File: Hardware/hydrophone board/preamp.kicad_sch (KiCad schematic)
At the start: 10 parts, among them U302 AD8541ARTZ

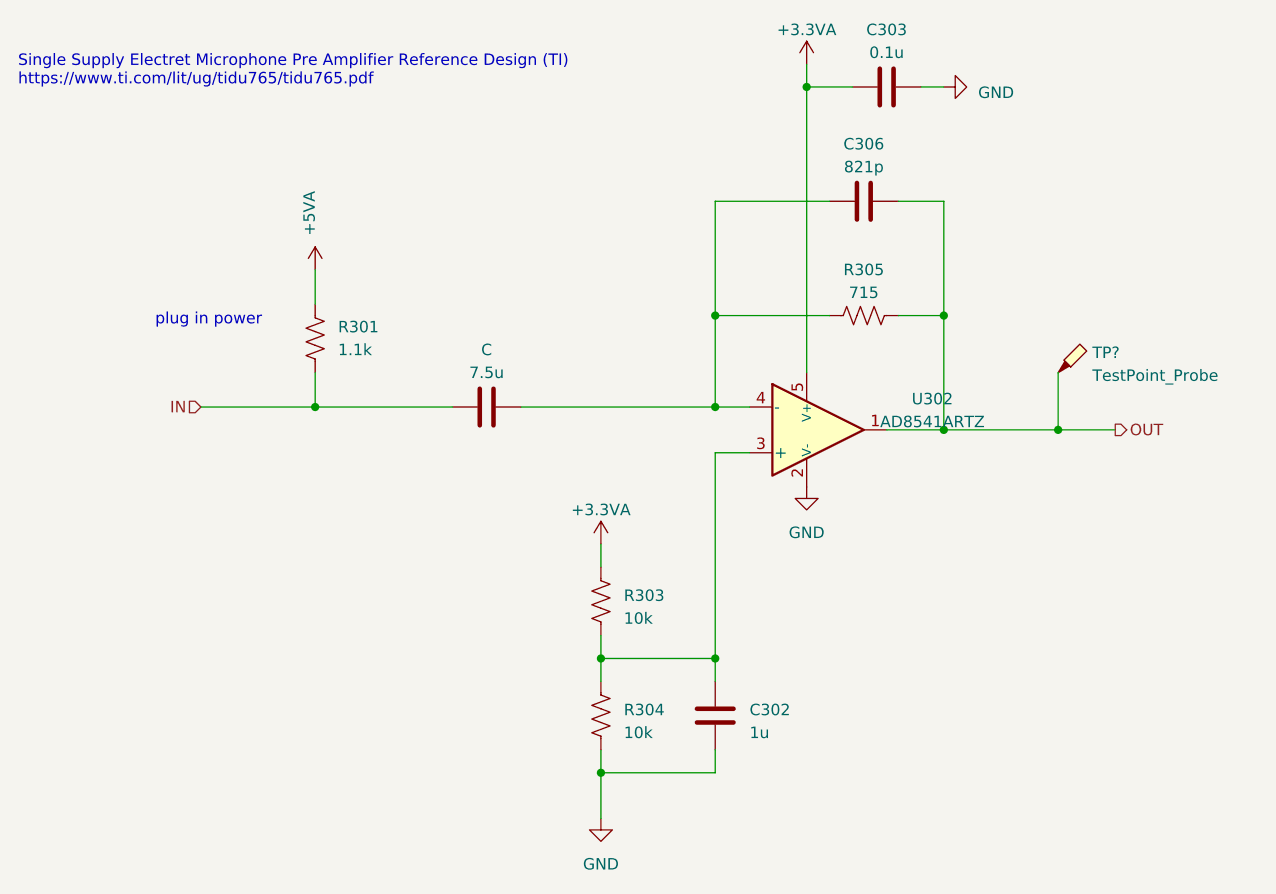
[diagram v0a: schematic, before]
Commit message: added teensy footprint
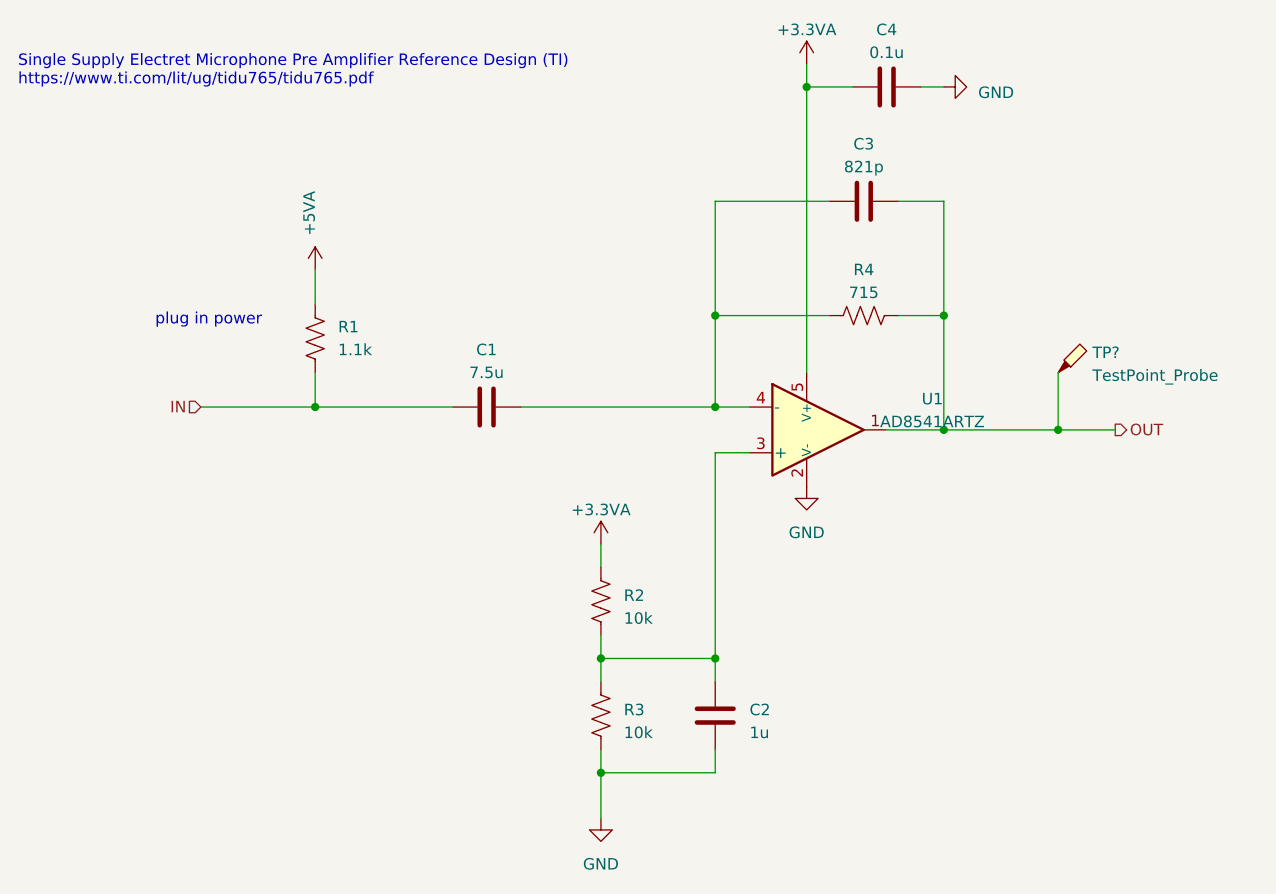
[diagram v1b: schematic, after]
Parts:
- renumbered C to C1, C302 to C2, C306 to C3, C303 to C4, R301 to R1, R303 to R2, R304 to R3, R305 to R4, U302 to U1
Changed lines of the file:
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@@
   (symbol (lib_id "power:+5VA") (at 63.5 71.12 0) (unit 1)
     (in_bom yes) (on_board yes) (dnp no) (fields_autoplaced)
-    (property "Reference" "#PWR0301" (at 63.5 74.93 0)
+    (property "Reference" "#PWR03" (at 63.5 74.93 0)
       (effects (font (size 1.27 1.27)) hide)
     )
@@
       (project "hydrophone board"
         (path "/4356d3a6-6a00-447d-897e-473f60221539/f560d530-135c-40dc-9144-4f9599a30f13"
-          (reference "#PWR0301") (unit 1)
+          (reference "#PWR03") (unit 1)
         )
       )
@@
   (symbol (lib_id "Device:C") (at 124.46 63.5 270) (unit 1)
     (in_bom yes) (on_board yes) (dnp no) (fields_autoplaced)
-    (property "Reference" "C306" (at 124.46 57.15 90)
+    (property "Reference" "C3" (at 124.46 57.15 90)
       (effects (font (size 1.27 1.27)))
     )
@@
       (project "hydrophone board"
         (path "/4356d3a6-6a00-447d-897e-473f60221539/f560d530-135c-40dc-9144-4f9599a30f13"
-          (reference "C306") (unit 1)
+          (reference "C3") (unit 1)
         )
       )
@@
         )
         (path "/4356d3a6-6a00-447d-897e-473f60221539/f560d530-135c-40dc-9144-4f9599a30f13"
-          (reference "#PWR0302") (unit 1)
+          (reference "#PWR04") (unit 1)
         )
       )
@@
         )
         (path "/4356d3a6-6a00-447d-897e-473f60221539/f560d530-135c-40dc-9144-4f9599a30f13"
-          (reference "#PWR0304") (unit 1)
+          (reference "#PWR06") (unit 1)
         )
       )
@@
   (symbol (lib_id "Device:R_US") (at 95.25 107.95 0) (unit 1)
     (in_bom yes) (on_board yes) (dnp no) (fields_autoplaced)
-    (property "Reference" "R303" (at 97.79 107.315 0)
+    (property "Reference" "R2" (at 97.79 107.315 0)
       (effects (font (size 1.27 1.27)) (justify left))
     )
@@
       (project "hydrophone board"
         (path "/4356d3a6-6a00-447d-897e-473f60221539/f560d530-135c-40dc-9144-4f9599a30f13"
-          (reference "R303") (unit 1)
+          (reference "R2") (unit 1)
         )
       )
@@
         )
         (path "/4356d3a6-6a00-447d-897e-473f60221539/f560d530-135c-40dc-9144-4f9599a30f13"
-          (reference "#PWR0305") (unit 1)
+          (reference "#PWR05") (unit 1)
         )
       )
@@
   (symbol (lib_id "Device:R_US") (at 124.46 76.2 90) (unit 1)
     (in_bom yes) (on_board yes) (dnp no) (fields_autoplaced)
-    (property "Reference" "R305" (at 124.46 71.12 90)
+    (property "Reference" "R4" (at 124.46 71.12 90)
       (effects (font (size 1.27 1.27)))
     )
@@
       (project "hydrophone board"
         (path "/4356d3a6-6a00-447d-897e-473f60221539/f560d530-135c-40dc-9144-4f9599a30f13"
-          (reference "R305") (unit 1)
+          (reference "R4") (unit 1)
         )
       )
@@
   (symbol (lib_id "Device:C") (at 82.55 86.36 90) (unit 1)
     (in_bom yes) (on_board yes) (dnp no) (fields_autoplaced)
-    (property "Reference" "C" (at 82.55 80.01 90)
+    (property "Reference" "C1" (at 82.55 80.01 90)
       (effects (font (size 1.27 1.27)))
     )
@@
       (project "hydrophone board"
         (path "/4356d3a6-6a00-447d-897e-473f60221539/f560d530-135c-40dc-9144-4f9599a30f13"
-          (reference "C") (unit 1)
+          (reference "C1") (unit 1)
         )
       )
@@
         )
         (path "/4356d3a6-6a00-447d-897e-473f60221539/f560d530-135c-40dc-9144-4f9599a30f13"
-          (reference "#PWR0303") (unit 1)
+          (reference "#PWR07") (unit 1)
         )
       )
@@
   (symbol (lib_id "Device:C") (at 107.95 120.65 180) (unit 1)
     (in_bom yes) (on_board yes) (dnp no) (fields_autoplaced)
-    (property "Reference" "C302" (at 111.76 120.015 0)
+    (property "Reference" "C2" (at 111.76 120.015 0)
       (effects (font (size 1.27 1.27)) (justify right))
     )
@@
       (project "hydrophone board"
         (path "/4356d3a6-6a00-447d-897e-473f60221539/f560d530-135c-40dc-9144-4f9599a30f13"
-          (reference "C302") (unit 1)
+          (reference "C2") (unit 1)
         )
       )
@@
   (symbol (lib_id "PCM_Amplifier_Operational_AKL:AD8541ARTZ") (at 119.38 88.9 0) (unit 1)
     (in_bom yes) (on_board yes) (dnp no) (fields_autoplaced)
-    (property "Reference" "U302" (at 132.08 85.4711 0)
+    (property "Reference" "U1" (at 132.08 85.4711 0)
       (effects (font (size 1.27 1.27)))
     )
@@
       (project "hydrophone board"
         (path "/4356d3a6-6a00-447d-897e-473f60221539/f560d530-135c-40dc-9144-4f9599a30f13"
-          (reference "U302") (unit 1)
+          (reference "U1") (unit 1)
         )
       )
@@
         )
         (path "/4356d3a6-6a00-447d-897e-473f60221539/f560d530-135c-40dc-9144-4f9599a30f13"
-          (reference "#PWR0307") (unit 1)
+          (reference "#PWR08") (unit 1)
         )
       )
@@
   (symbol (lib_id "Device:C") (at 127 50.8 90) (unit 1)
     (in_bom yes) (on_board yes) (dnp no) (fields_autoplaced)
-    (property "Reference" "C303" (at 127 44.45 90)
+    (property "Reference" "C4" (at 127 44.45 90)
       (effects (font (size 1.27 1.27)))
     )
@@
       (project "hydrophone board"
         (path "/4356d3a6-6a00-447d-897e-473f60221539/f560d530-135c-40dc-9144-4f9599a30f13"
-          (reference "C303") (unit 1)
+          (reference "C4") (unit 1)
         )
       )
@@
         )
         (path "/4356d3a6-6a00-447d-897e-473f60221539/f560d530-135c-40dc-9144-4f9599a30f13"
-          (reference "TP301") (unit 1)
+          (reference "TP1") (unit 1)
         )
       )
@@
   (symbol (lib_id "Device:R_US") (at 63.5 78.74 180) (unit 1)
     (in_bom yes) (on_board yes) (dnp no)
-    (property "Reference" "R301" (at 66.04 77.47 0)
+    (property "Reference" "R1" (at 66.04 77.47 0)
       (effects (font (size 1.27 1.27)) (justify right))
     )
@@
       (project "hydrophone board"
         (path "/4356d3a6-6a00-447d-897e-473f60221539/f560d530-135c-40dc-9144-4f9599a30f13"
-          (reference "R301") (unit 1)
+          (reference "R1") (unit 1)
         )
       )
@@
   (symbol (lib_id "Device:R_US") (at 95.25 120.65 0) (unit 1)
     (in_bom yes) (on_board yes) (dnp no) (fields_autoplaced)
-    (property "Reference" "R304" (at 97.79 120.015 0)
+    (property "Reference" "R3" (at 97.79 120.015 0)
       (effects (font (size 1.27 1.27)) (justify left))
     )
@@
       (project "hydrophone board"
         (path "/4356d3a6-6a00-447d-897e-473f60221539/f560d530-135c-40dc-9144-4f9599a30f13"
-          (reference "R304") (unit 1)
-        )
-      )
+          (reference "R3") (unit 1)
+        )
+      )

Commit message: annotate all component
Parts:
- renumbered C4 to C111, C3 to C112, C1 to C113, C2 to C114, R4 to R111, R1 to R112, R2 to R113, R3 to R114, U1 to U111

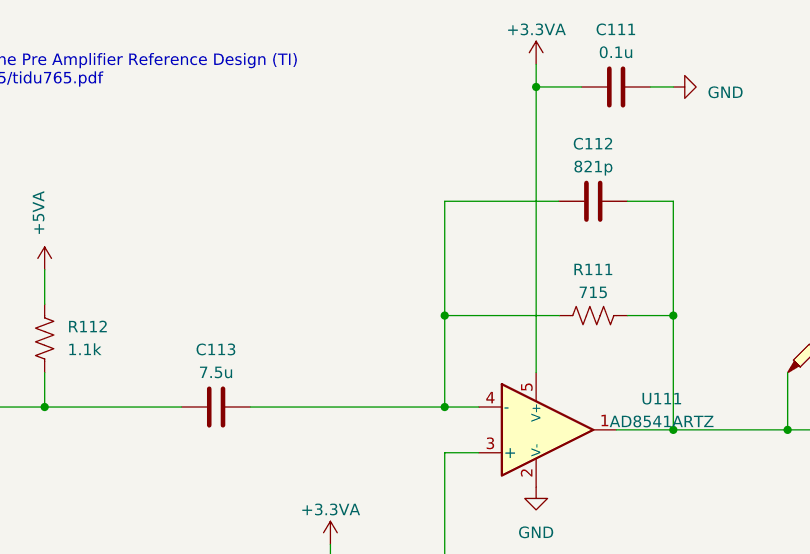
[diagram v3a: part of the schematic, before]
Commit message: assigned footprints
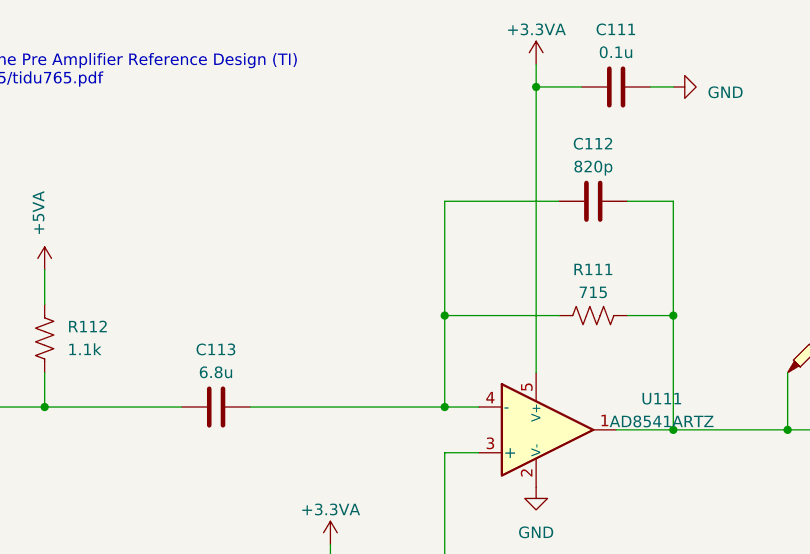
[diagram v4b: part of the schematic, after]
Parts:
- C111, C114: footprint (none) -> Capacitor_SMD:C_0603_1608Metric
- C112: value 821p -> 820p; footprint (none) -> Capacitor_SMD:C_0603_1608Metric
- C113: value 7.5u -> 6.8u; footprint (none) -> Capacitor_SMD:C_0805_2012Metric
- R111, R112, R113, R114: footprint (none) -> Resistor_SMD:R_0603_1608Metric
- TP?: footprint (none) -> Connector_PinHeader_2.54mm:PinHeader_1x01_P2.54mm_Vertical
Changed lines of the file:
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@@
       (effects (font (size 1.27 1.27)))
     )
-    (property "Value" "821p" (at 124.46 59.69 90)
-      (effects (font (size 1.27 1.27)))
-    )
-    (property "Footprint" "" (at 120.65 64.4652 0)
+    (property "Value" "820p" (at 124.46 59.69 90)
+      (effects (font (size 1.27 1.27)))
+    )
+    (property "Footprint" "Capacitor_SMD:C_0603_1608Metric" (at 120.65 64.4652 0)
       (effects (font (size 1.27 1.27)) hide)
     )
@@
       (effects (font (size 1.27 1.27)) (justify left))
     )
-    (property "Footprint" "" (at 96.266 108.204 90)
+    (property "Footprint" "Resistor_SMD:R_0603_1608Metric" (at 96.266 108.204 90)
       (effects (font (size 1.27 1.27)) hide)
     )
@@
       (effects (font (size 1.27 1.27)))
     )
-    (property "Footprint" "" (at 124.714 75.184 90)
+    (property "Footprint" "Resistor_SMD:R_0603_1608Metric" (at 124.714 75.184 90)
       (effects (font (size 1.27 1.27)) hide)
     )
@@
       (effects (font (size 1.27 1.27)))
     )
-    (property "Value" "7.5u" (at 82.55 82.55 90)
-      (effects (font (size 1.27 1.27)))
-    )
-    (property "Footprint" "" (at 86.36 85.3948 0)
+    (property "Value" "6.8u" (at 82.55 82.55 90)
+      (effects (font (size 1.27 1.27)))
+    )
+    (property "Footprint" "Capacitor_SMD:C_0805_2012Metric" (at 86.36 85.3948 0)
       (effects (font (size 1.27 1.27)) hide)
     )
@@
       (effects (font (size 1.27 1.27)) (justify right))
     )
-    (property "Footprint" "" (at 106.9848 116.84 0)
+    (property "Footprint" "Capacitor_SMD:C_0603_1608Metric" (at 106.9848 116.84 0)
       (effects (font (size 1.27 1.27)) hide)
     )
@@
       (effects (font (size 1.27 1.27)))
     )
-    (property "Footprint" "" (at 130.81 49.8348 0)
+    (property "Footprint" "Capacitor_SMD:C_0603_1608Metric" (at 130.81 49.8348 0)
       (effects (font (size 1.27 1.27)) hide)
     )
@@
       (effects (font (size 1.27 1.27)) (justify left))
     )
-    (property "Footprint" "" (at 151.13 82.55 0)
+    (property "Footprint" "Connector_PinHeader_2.54mm:PinHeader_1x01_P2.54mm_Vertical" (at 151.13 82.55 0)
       (effects (font (size 1.27 1.27)) hide)
     )
@@
       (effects (font (size 1.27 1.27)) (justify right))
     )
-    (property "Footprint" "" (at 62.484 78.486 90)
+    (property "Footprint" "Resistor_SMD:R_0603_1608Metric" (at 62.484 78.486 90)
       (effects (font (size 1.27 1.27)) hide)
     )
@@
       (effects (font (size 1.27 1.27)) (justify left))
     )
-    (property "Footprint" "" (at 96.266 120.904 90)
-      (effects (font (size 1.27 1.27)) hide)
-    )
+    (property "Footprint" "Resistor_SMD:R_0603_1608Metric" (at 96.266 120.904 90)
+      (effects (font (size 1.27 1.27)) hide)
+    )

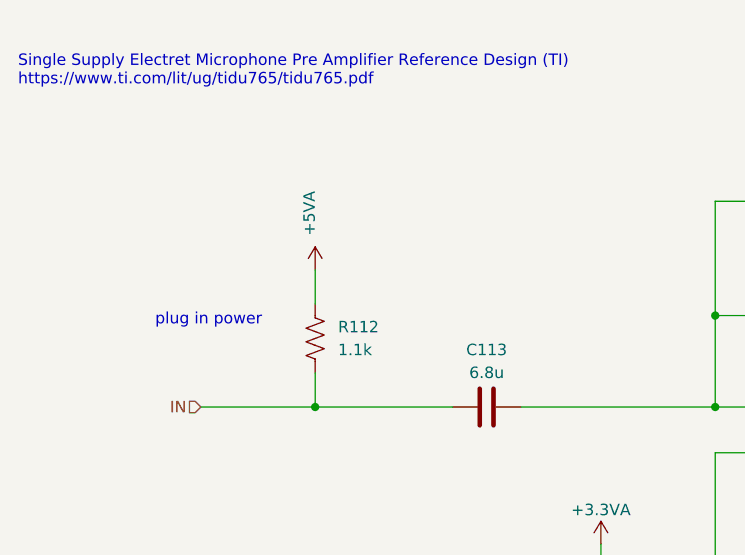
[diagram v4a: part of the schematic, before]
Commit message: resolved ERC errors and changed mic bias resistor for 3.3V
1.1k -> 360 ohm
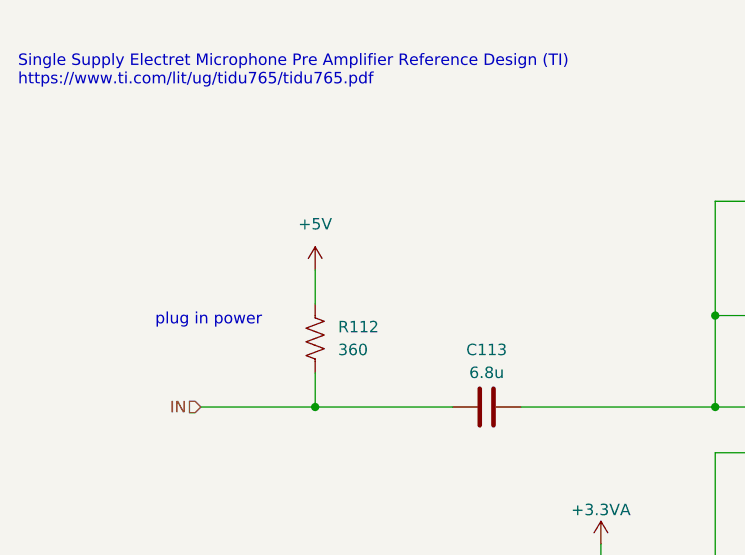
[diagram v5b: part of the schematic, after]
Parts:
- R112: value 1.1k -> 360
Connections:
- net +5VA renamed +5V
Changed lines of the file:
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@@
     (effects (font (size 1.27 1.27)) (justify left))
   )
-  (symbol (lib_id "power:+5VA") (at 63.5 71.12 0) (unit 1)
-    (in_bom yes) (on_board yes) (dnp no) (fields_autoplaced)
-    (property "Reference" "#PWR0113" (at 63.5 74.93 0)
-      (effects (font (size 1.27 1.27)) hide)
-    )
-    (property "Value" "+5VA" (at 62.865 67.31 90)
-      (effects (font (size 1.27 1.27)) (justify left))
+  (symbol (lib_id "Device:C") (at 124.46 63.5 270) (unit 1)
+    (in_bom yes) (on_board yes) (dnp no) (fields_autoplaced)
+    (property "Reference" "C112" (at 124.46 57.15 90)
+      (effects (font (size 1.27 1.27)))
+    )
+    (property "Value" "820p" (at 124.46 59.69 90)
+      (effects (font (size 1.27 1.27)))
+    )
+    (property "Footprint" "Capacitor_SMD:C_0603_1608Metric" (at 120.65 64.4652 0)
+      (effects (font (size 1.27 1.27)) hide)
+    )
+    (property "Datasheet" "~" (at 124.46 63.5 0)
+      (effects (font (size 1.27 1.27)) hide)
+    )
+    (pin "1")
+    (pin "2")
+    (instances
+      (project "hydrophone board"
+        (path "/4356d3a6-6a00-447d-897e-473f60221539/f560d530-135c-40dc-9144-4f9599a30f13"
+          (reference "C112") (unit 1)
+        )
+        (path "/4356d3a6-6a00-447d-897e-473f60221539/fa1a46a1-ed86-4a84-a182-b5dbe7fc86e7"
+          (reference "C122") (unit 1)
+        )
+        (path "/4356d3a6-6a00-447d-897e-473f60221539/d3a562a3-af99-4bb5-b5fa-eb83660cffa4"
+          (reference "C132") (unit 1)
+        )
+        (path "/4356d3a6-6a00-447d-897e-473f60221539/6f981a72-1f6f-4ccf-ba7d-c5dfb70b4229"
+          (reference "C142") (unit 1)
+        )
+      )
+    )
+  )
+  (symbol (lib_id "PCM_4ms_Power-symbol:+5V") (at 63.5 71.12 0) (unit 1)
+    (in_bom yes) (on_board yes) (dnp no) (fields_autoplaced)
+    (property "Reference" "#PWR0248" (at 63.5 74.93 0)
+      (effects (font (size 1.27 1.27)) hide)
+    )
+    (property "Value" "+5V" (at 63.5 66.04 0)
+      (effects (font (size 1.27 1.27)))
     )
     (property "Footprint" "" (at 63.5 71.12 0)
@@
       (project "hydrophone board"
         (path "/4356d3a6-6a00-447d-897e-473f60221539/f560d530-135c-40dc-9144-4f9599a30f13"
-          (reference "#PWR0113") (unit 1)
-        )
-        (path "/4356d3a6-6a00-447d-897e-473f60221539/fa1a46a1-ed86-4a84-a182-b5dbe7fc86e7"
-          (reference "#PWR0123") (unit 1)
-        )
-        (path "/4356d3a6-6a00-447d-897e-473f60221539/d3a562a3-af99-4bb5-b5fa-eb83660cffa4"
-          (reference "#PWR0133") (unit 1)
-        )
-        (path "/4356d3a6-6a00-447d-897e-473f60221539/6f981a72-1f6f-4ccf-ba7d-c5dfb70b4229"
-          (reference "#PWR0143") (unit 1)
-        )
-      )
-    )
-  )
-  (symbol (lib_id "Device:C") (at 124.46 63.5 270) (unit 1)
-    (in_bom yes) (on_board yes) (dnp no) (fields_autoplaced)
-    (property "Reference" "C112" (at 124.46 57.15 90)
-      (effects (font (size 1.27 1.27)))
-    )
-    (property "Value" "820p" (at 124.46 59.69 90)
-      (effects (font (size 1.27 1.27)))
-    )
-    (property "Footprint" "Capacitor_SMD:C_0603_1608Metric" (at 120.65 64.4652 0)
-      (effects (font (size 1.27 1.27)) hide)
-    )
-    (property "Datasheet" "~" (at 124.46 63.5 0)
-      (effects (font (size 1.27 1.27)) hide)
-    )
-    (pin "1")
-    (pin "2")
-    (instances
-      (project "hydrophone board"
-        (path "/4356d3a6-6a00-447d-897e-473f60221539/f560d530-135c-40dc-9144-4f9599a30f13"
-          (reference "C112") (unit 1)
-        )
-        (path "/4356d3a6-6a00-447d-897e-473f60221539/fa1a46a1-ed86-4a84-a182-b5dbe7fc86e7"
-          (reference "C122") (unit 1)
-        )
-        (path "/4356d3a6-6a00-447d-897e-473f60221539/d3a562a3-af99-4bb5-b5fa-eb83660cffa4"
-          (reference "C132") (unit 1)
-        )
-        (path "/4356d3a6-6a00-447d-897e-473f60221539/6f981a72-1f6f-4ccf-ba7d-c5dfb70b4229"
-          (reference "C142") (unit 1)
+          (reference "#PWR0248") (unit 1)
+        )
+        (path "/4356d3a6-6a00-447d-897e-473f60221539/fa1a46a1-ed86-4a84-a182-b5dbe7fc86e7"
+          (reference "#PWR0249") (unit 1)
+        )
+        (path "/4356d3a6-6a00-447d-897e-473f60221539/d3a562a3-af99-4bb5-b5fa-eb83660cffa4"
+          (reference "#PWR0250") (unit 1)
+        )
+        (path "/4356d3a6-6a00-447d-897e-473f60221539/6f981a72-1f6f-4ccf-ba7d-c5dfb70b4229"
+          (reference "#PWR0251") (unit 1)
         )
       )
@@
       (effects (font (size 1.27 1.27)) (justify right))
     )
-    (property "Value" "1.1k" (at 66.04 80.01 0)
+    (property "Value" "360" (at 66.04 80.01 0)
       (effects (font (size 1.27 1.27)) (justify right))
     )
